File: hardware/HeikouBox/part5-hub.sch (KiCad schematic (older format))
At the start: 43 parts, among them J501 USB_B_Micro, J502 Micro_SD_Card_Det, Q501 MMBT3906, SW501 SW_Push, SW502 SW_Push, SW503 SW_Push, SW504 SW_Push, U501 ATmega644PA-AU, U502 MCP2221AxSL, Y501 8MHz

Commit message: Replace MCU with blue pill, tidy up
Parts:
- removed C501, C505, C506, C509, C511, C512: 100n, Capacitor_SMD:C_0603_1608Metric_Pad1.05x0.95mm_HandSolder, symbol Device:C
- removed C507, C508: 22p, Capacitor_SMD:C_0603_1608Metric_Pad1.05x0.95mm_HandSolder, symbol Device:C
- removed D501: RX, LED_SMD:LED_0603_1608Metric_Pad1.05x0.95mm_HandSolder, symbol Device:LED
- removed D502: TX, LED_SMD:LED_0603_1608Metric_Pad1.05x0.95mm_HandSolder, symbol Device:LED
- removed D503: LOAD, LED_SMD:LED_0603_1608Metric_Pad1.05x0.95mm_HandSolder, symbol Device:LED
- removed J501: USB_B_Micro, KSK_HeikouBox:USB_Mini-Micro-B_Multi, symbol Connector:USB_B_Micro
- removed Q501: MMBT3906, Package_TO_SOT_SMD:SOT-23, symbol Transistor_BJT:MMBT3906
- removed R502, R509: 1K, Resistor_SMD:R_0603_1608Metric_Pad1.05x0.95mm_HandSolder, symbol Device:R
- removed R513: 10K, Resistor_SMD:R_0603_1608Metric_Pad1.05x0.95mm_HandSolder, symbol Device:R
- removed R98: 2K2, Resistor_SMD:R_0603_1608Metric_Pad1.05x0.95mm_HandSolder, symbol Device:R
- removed RN501, RN502: 2K2, Resistor_SMD:R_Array_Convex_4x0603, symbol Device:R_Pack04_Split
- removed SW501: SW_Push, Button_Switch_THT:SW_PUSH_6mm_H5mm, symbol Switch:SW_Push
- removed U501: ATmega644PA-AU, Package_QFP:TQFP-44_10x10mm_P0.8mm, symbol MCU_Microchip_ATmega:ATmega644PA-AU
- removed U502: MCP2221AxSL, Package_SO:SOIC-14_3.9x8.7mm_P1.27mm, symbol Interface_USB:MCP2221AxSL
- removed Y501: 8MHz, Crystal:Crystal_HC49-4H_Vertical, symbol Device:Crystal
- added D501: WS2812B, LED_SMD:LED_WS2812B_PLCC4_5.0x5.0mm_P3.2mm, symbol LED:WS2812B
- added J502: RGB, symbol Connector_Generic:Conn_01x03
- added JP501: Test, symbol Jumper:SolderJumper_2_Open
- added JP502: DVCC, symbol Jumper:SolderJumper_3_Bridged12
- added JP503: DGND, symbol Jumper:SolderJumper_3_Bridged12
- added R502: RUSB, Resistor_SMD:R_0603_1608Metric_Pad1.05x0.95mm_HandSolder, symbol Device:R
- added R502, R504, R506, R515, R517, R519: 1K, Resistor_SMD:R_0603_1608Metric_Pad1.05x0.95mm_HandSolder, symbol Device:R
- added R516, R518: 10K, Resistor_SMD:R_0603_1608Metric_Pad1.05x0.95mm_HandSolder, symbol Device:R
- added R520: 100R, Resistor_SMD:R_0603_1608Metric_Pad1.05x0.95mm_HandSolder, symbol Device:R
- added SW502: Down, Button_Switch_THT:SW_PUSH_6mm_H5mm, symbol Switch:SW_Push
- added U501: STM32-BluePill-Socket, symbol KSK_HeikouBox:STM32-BluePill-Socket
- R509: renamed from R504; value 1K -> 10K
- R510: value 1K -> 2K2
- R511: value 10K -> 2K2
- SW501: renamed from SW502; value SW_Push -> Up
- SW503: value SW_Push -> Left
- SW504: value SW_Push -> Right
- renumbered C510 to C501, J502 to J501, R506 to R513, DS501 to U502
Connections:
- net labels added: cfg_DONE
- net labels removed: gp_CLK, gp_D1, gp_D2, gp_LAT, kb_C, kb_D
- wire segments 164 -> 134
- no-connect marks 8 -> 7
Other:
- note added: "I2C1_SCL"
- note added: "I2C1_SDA"
- note added: "RUSB depends on existing pullup on blue pill!\nNone -> RUSB=1K5\n10K -> RUSB=1K8\n4K7 -> RUSB=2K2\n1K5 -> RUSB=None"
- note added: "SD card"
- note added: "SPI1_MISO"
- note added: "SPI1_MOSI"
- note added: "SPI1_NSS"
- note added: "SPI1_SCK"
- note added: "SPI2_MOSI"
- note added: "SPI2_SCK"
- note added: "STM32 Blue Pill"
- note added: "UART1_RX"
- note added: "UART1_TX"
- note removed: "8M"
- note removed: "Down"
- note removed: "LED PIN"
- note removed: "MISO"
- note removed: "MOSI"
- note removed: "Place near MCP2221"
- note removed: "Place near MCU"
- note removed: "RXD0"
- note removed: "RXD1"
- note removed: "Reset"
- note removed: "SCL"
- note removed: "SD Card"
- note removed: "SDA"
- note removed: "SS"
- note removed: "Select"
- note removed: "TXD0"
- note removed: "TXD1"
- note removed: "USB"
- note removed: "Up"
- note removed: "XCK1"
- moved on the sheet: C501, J501, R509, R512, R513, SW501, U502

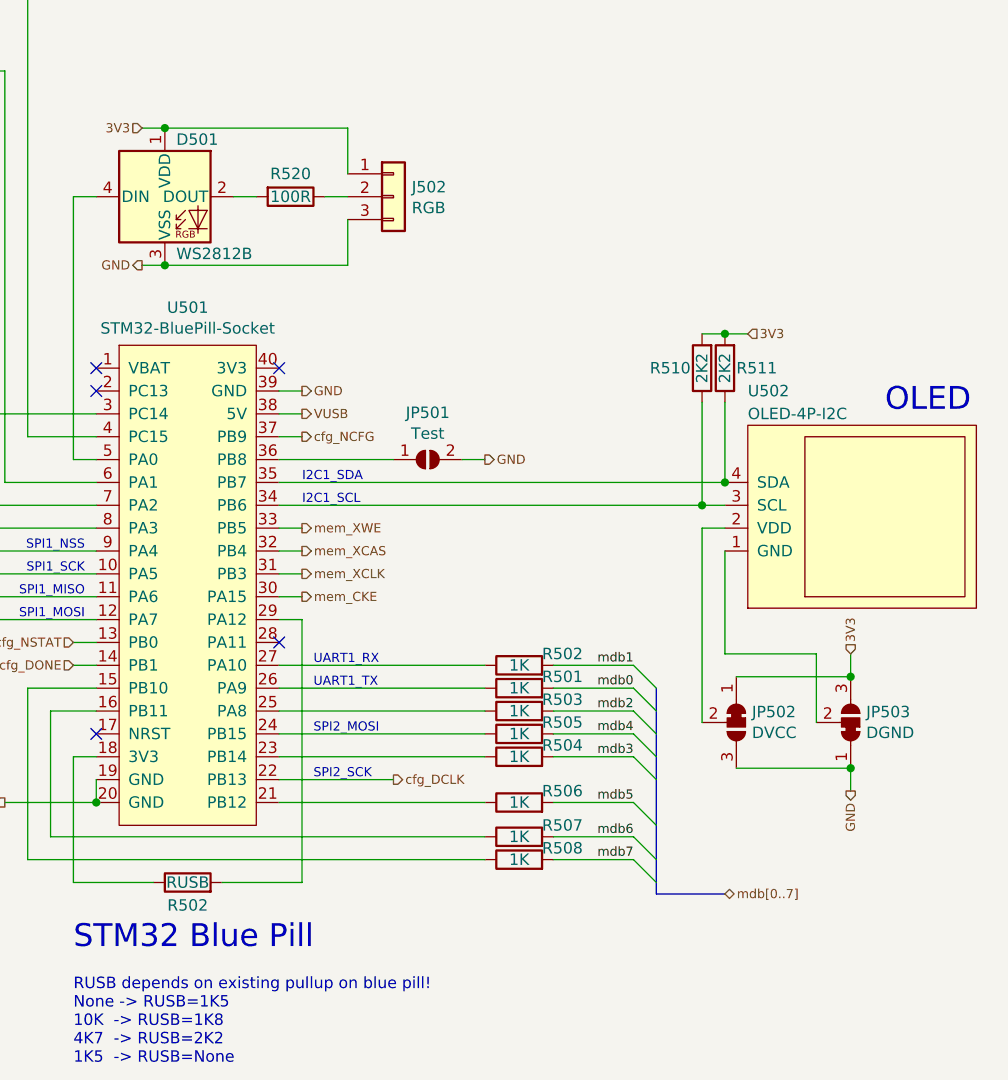
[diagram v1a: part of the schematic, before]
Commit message: Fix DRC, make netlist
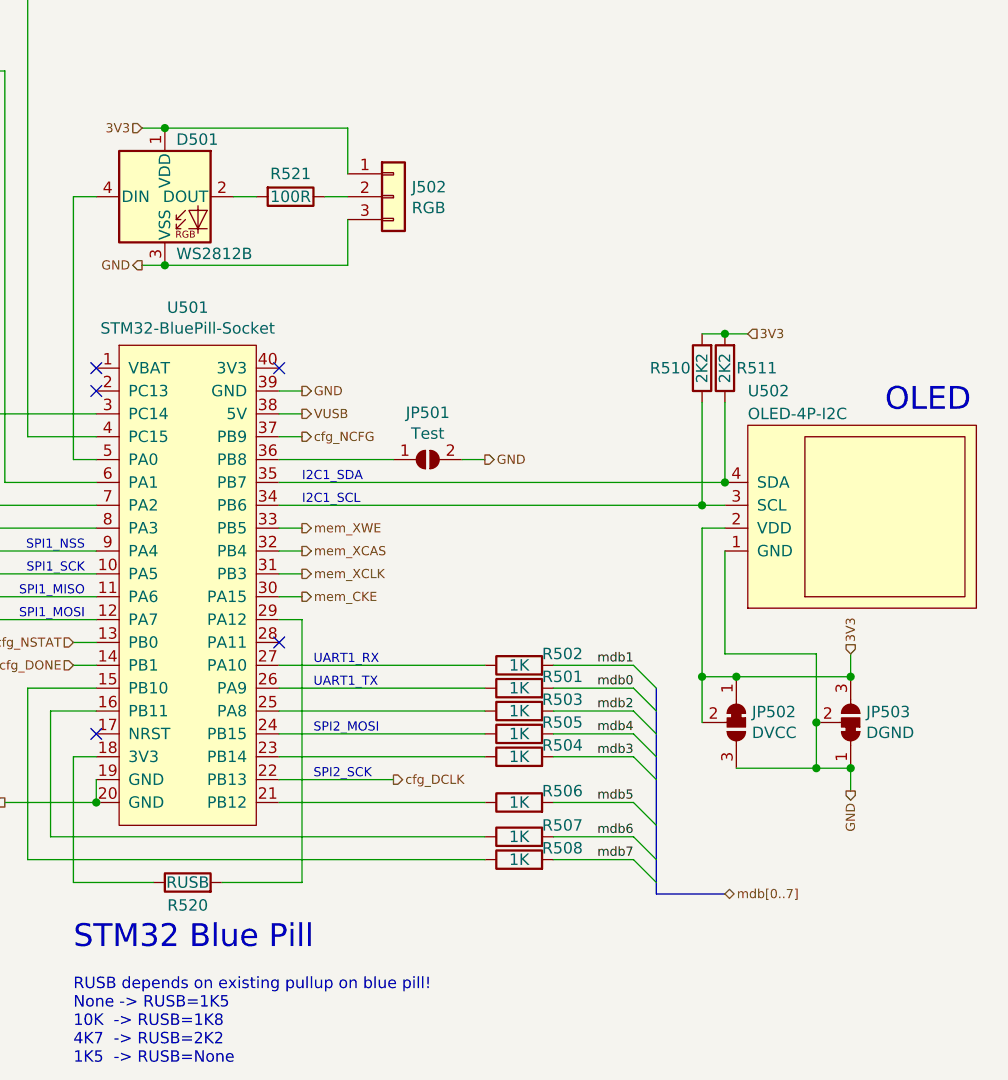
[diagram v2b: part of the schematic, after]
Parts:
- renumbered R502 to R520, R520 to R521
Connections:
- net 3V3: now also JP502.2 (C), U502.2 (VDD)
- net GND: now also JP503.2 (C), U502.1 (GND)
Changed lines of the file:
@@
 $Descr A4 11693 8268
 encoding utf-8
-Sheet 6 6
+Sheet 2 6
 Title "HeikouBox Mainboard - Hub"
 Date "2021-03-17"
@@
 P 4000 4950
 AR Path="/630A62EE" Ref="R?"  Part="1"
-AR Path="/646E3FCF/630A62EE" Ref="R502"  Part="1"
-F 0 "R502" V 3900 4950 50  0000 C CNN
+AR Path="/646E3FCF/630A62EE" Ref="R520"  Part="1"
+F 0 "R520" V 3900 4950 50  0000 C CNN
 F 1 "RUSB" V 4000 4950 50  0000 C CNN
 F 2 "Resistor_SMD:R_0603_1608Metric_Pad1.05x0.95mm_HandSolder" V 3930 4950 50  0001 C CNN
@@
 P 4450 1950
 AR Path="/640DEF09" Ref="R?"  Part="1"
-AR Path="/646E3FCF/640DEF09" Ref="R520"  Part="1"
-F 0 "R520" V 4350 1950 50  0000 C CNN
+AR Path="/646E3FCF/640DEF09" Ref="R521"  Part="1"
+F 0 "R521" V 4350 1950 50  0000 C CNN
 F 1 "100R" V 4450 1950 50  0000 C CNN
 F 2 "Resistor_SMD:R_0603_1608Metric_Pad1.05x0.95mm_HandSolder" V 4380 1950 50  0001 C CNN
@@
 	6400 4050 6900 4050
 Wire Wire Line
-	6400 4450 6900 4450
+	6400 4450 6750 4450
 Connection ~ 6900 4450
 Connection ~ 6900 4050
 Wire Wire Line
-	6250 3400 6250 4250
+	6250 3400 6250 4050
 Wire Wire Line
 	6250 3400 6350 3400
@@
 Wire Wire Line
 	6350 3500 6350 3950
+Wire Wire Line
+	4400 3200 6350 3200
+Wire Wire Line
+	4400 3300 6250 3300
+Wire Wire Line
+	6400 4050 6250 4050
+Connection ~ 6400 4050
+Connection ~ 6250 4050
+Wire Wire Line
+	6250 4050 6250 4250
+Wire Wire Line
+	6750 4250 6750 4450
 Wire Bus Line
 	6050 4100 6050 5000
-Wire Wire Line
-	4400 3200 6350 3200
-Wire Wire Line
-	4400 3300 6250 3300
+Connection ~ 6750 4250
+Connection ~ 6750 4450
+Wire Wire Line
+	6750 4450 6900 4450
 $EndSCHEMATC

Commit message: Mostly routed board
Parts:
- added D502, D503, D504: WS2812B, LED_SMD:LED_WS2812B_PLCC4_5.0x5.0mm_P3.2mm, symbol LED:WS2812B
- added J503: PS/2, KSK_HeikouBox:TE_Mini-DIN-6_Horizontal, symbol KSK_HeikouBox:Mini-DIN-6_Shielded
- added Q501, Q502, Q503: BSS138, Package_TO_SOT_SMD:SOT-23, symbol Transistor_FET:BSS138
- added R522, R523, R524: 1K, Resistor_SMD:R_0603_1608Metric_Pad0.98x0.95mm_HandSolder, symbol Device:R
- added R525, R526, R527, R528: 10K, Resistor_SMD:R_0603_1608Metric_Pad0.98x0.95mm_HandSolder, symbol Device:R
- C501, C502, C503, C504: footprint Capacitor_SMD:C_0603_1608Metric_Pad1.05x0.95mm_HandSolder -> Capacitor_SMD:C_0603_1608Metric_Pad1.08x0.95mm_HandSolder
- DS501: renamed from U502; footprint KSK_HeikouBox:OLED-4P-Generic-128x32-0.91in -> KSK_HeikouBox:OLED-4P-Generic-128x64-0.96in
- J501: value Micro_SD_Card_Det -> Micro_SD_Card_TFP09-2-12B; footprint Connector_Card:microSD_HC_Hirose_DM3D-SF -> KSK_HeikouBox:Micro_SD_Card_TFP09-2-12B; symbol Connector:Micro_SD_Card_Det -> KSK_HeikouBox:Micro_SD_Card_TFP09-2-12B
- J502: footprint (none) -> Connector_PinHeader_2.54mm:PinHeader_1x03_P2.54mm_Vertical
- JP501: value Test -> RGB Bypass; footprint (none) -> Jumper:SolderJumper-2_P1.3mm_Open_RoundedPad1.0x1.5mm
- JP502, JP503: footprint (none) -> Jumper:SolderJumper-3_P1.3mm_Open_RoundedPad1.0x1.5mm; symbol Jumper:SolderJumper_3_Bridged12 -> Jumper:SolderJumper_3_Open
- R501, R502, R503, R504, R505, R506, R507, R508, R509, R510, R511, R512, R513, R514, R515, R516, R517, R518, R519, R520: footprint Resistor_SMD:R_0603_1608Metric_Pad1.05x0.95mm_HandSolder -> Resistor_SMD:R_0603_1608Metric_Pad0.98x0.95mm_HandSolder
- R521: value 100R -> 1K; footprint Resistor_SMD:R_0603_1608Metric_Pad1.05x0.95mm_HandSolder -> Resistor_SMD:R_0603_1608Metric_Pad0.98x0.95mm_HandSolder
- SW501: value Up -> Left
- SW502: value Down -> Up
- SW503: value Left -> Down
- U501: footprint (none) -> KSK_HeikouBox:STM32-BluePill-Socket
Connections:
- net 3V3: now also R512.1, R514.1, R516.1, R518.1, R520.2, R521.2, Q501.1 (G), Q502.1 (G), Q503.1 (G), R525.2, R527.2; no longer D501.1 (VDD), DS501.2 (VDD), J502.1 (Pin_1), JP502.2 (C), R512.2, R514.2, R516.2, R518.2
- net GND: now also SW501.2, SW502.2, SW503.2, SW504.2, D502.3 (VSS), D503.3 (VSS), D504.3 (VSS), J503.3, J503.SH; no longer DS501.1 (GND), J501.10 (DET_A), J501.11 (SHIELD), JP501.2 (B), JP503.2 (C), R513.1, R515.1, R517.1, R519.1
- net cfg_DONE: now also U501.32 (PB4); no longer U501.14 (PB1)
- net cfg_NSTAT: now also U501.33 (PB5); no longer U501.13 (PB0)
- net mem_XCAS: now also U501.31 (PB3); no longer U501.32 (PB4)
- net mem_XCLK: now also U501.13 (PB0); no longer U501.31 (PB3)
- net mem_XWE: now also U501.14 (PB1); no longer U501.33 (PB5)
- net at U501.18 (3V3): no longer R520.1
- net at U501.2 (PC13): now also Q502.2 (S), R525.1
- net at U501.29 (PA12): now also R520.1; no longer R520.2
- net at U501.36 (PB8): now also Q503.2 (S), R527.1; no longer JP501.1 (A)
- net at C501.2, U501.4 (PC15): now also R512.2, R513.2; no longer R512.1, SW501.1
- net at U501.5 (PA0): now also R521.1, Q501.2 (S); no longer D501.4 (DIN)
- net at C502.2, U501.6 (PA1): now also R514.2, R515.2; no longer R514.1, SW502.1
- net at C503.2, U501.7 (PA2): now also R516.2, R517.2; no longer R516.1, SW503.1
- net at C504.2, U501.8 (PA3): now also R518.2, R519.2; no longer R518.1, SW504.1
- net at D501.2 (DOUT): now also D502.4 (DIN); no longer R521.2
- net at J502.2 (Pin_2): now also JP501.2 (B), R524.2; no longer R521.1
- new net: J503.1, Q502.3 (D), R526.1
- new net: J503.5, Q503.3 (D), R528.1
- new net: D502.2 (DOUT), D503.4 (DIN)
- new net: D503.2 (DOUT), D504.4 (DIN)
- new net: D504.2 (DOUT), R524.1
- new net: R515.1, SW502.1
- new net: R517.1, SW503.1
- new net: R519.1, SW504.1
- new net: Q501.3 (D), R522.1, R523.1
- new net: D501.4 (DIN), JP501.1 (A), R523.2
- new net: DS501.2 (VDD), JP502.2 (C)
- new net: DS501.1 (GND), JP503.2 (C)
- new net: R513.1, SW501.1
- new net 5V: D501.1 (VDD), D502.1 (VDD), D503.1 (VDD), D504.1 (VDD), J502.1 (Pin_1), J503.4, R522.2, R526.2, R528.2
- no-connect marks 7 -> 9
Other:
- note added: "Gamer RGB go-faster lights"
- note added: "Keyboard"
- note added: "PS/2 Clock"
- note added: "PS/2 Data"
- moved on the sheet: C501, C502, C503, C504, D501, DS501, J502, R501, R502, R503, R504, R505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

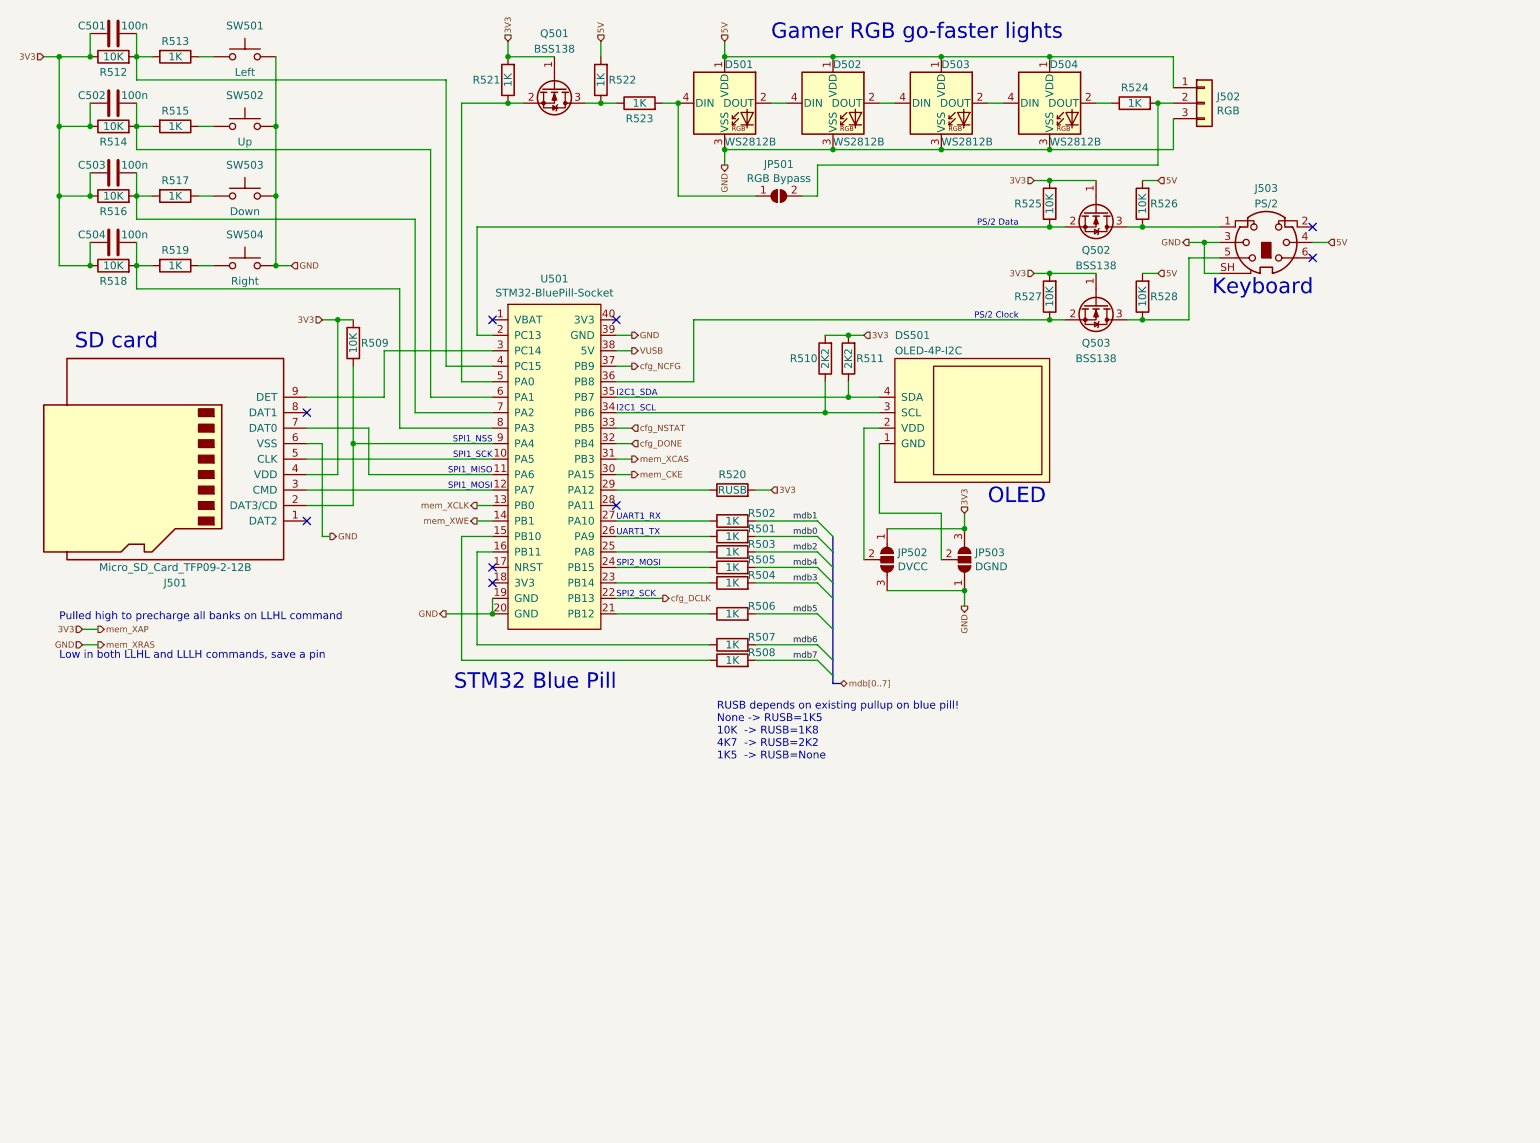
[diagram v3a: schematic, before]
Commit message: Rerouted some logic
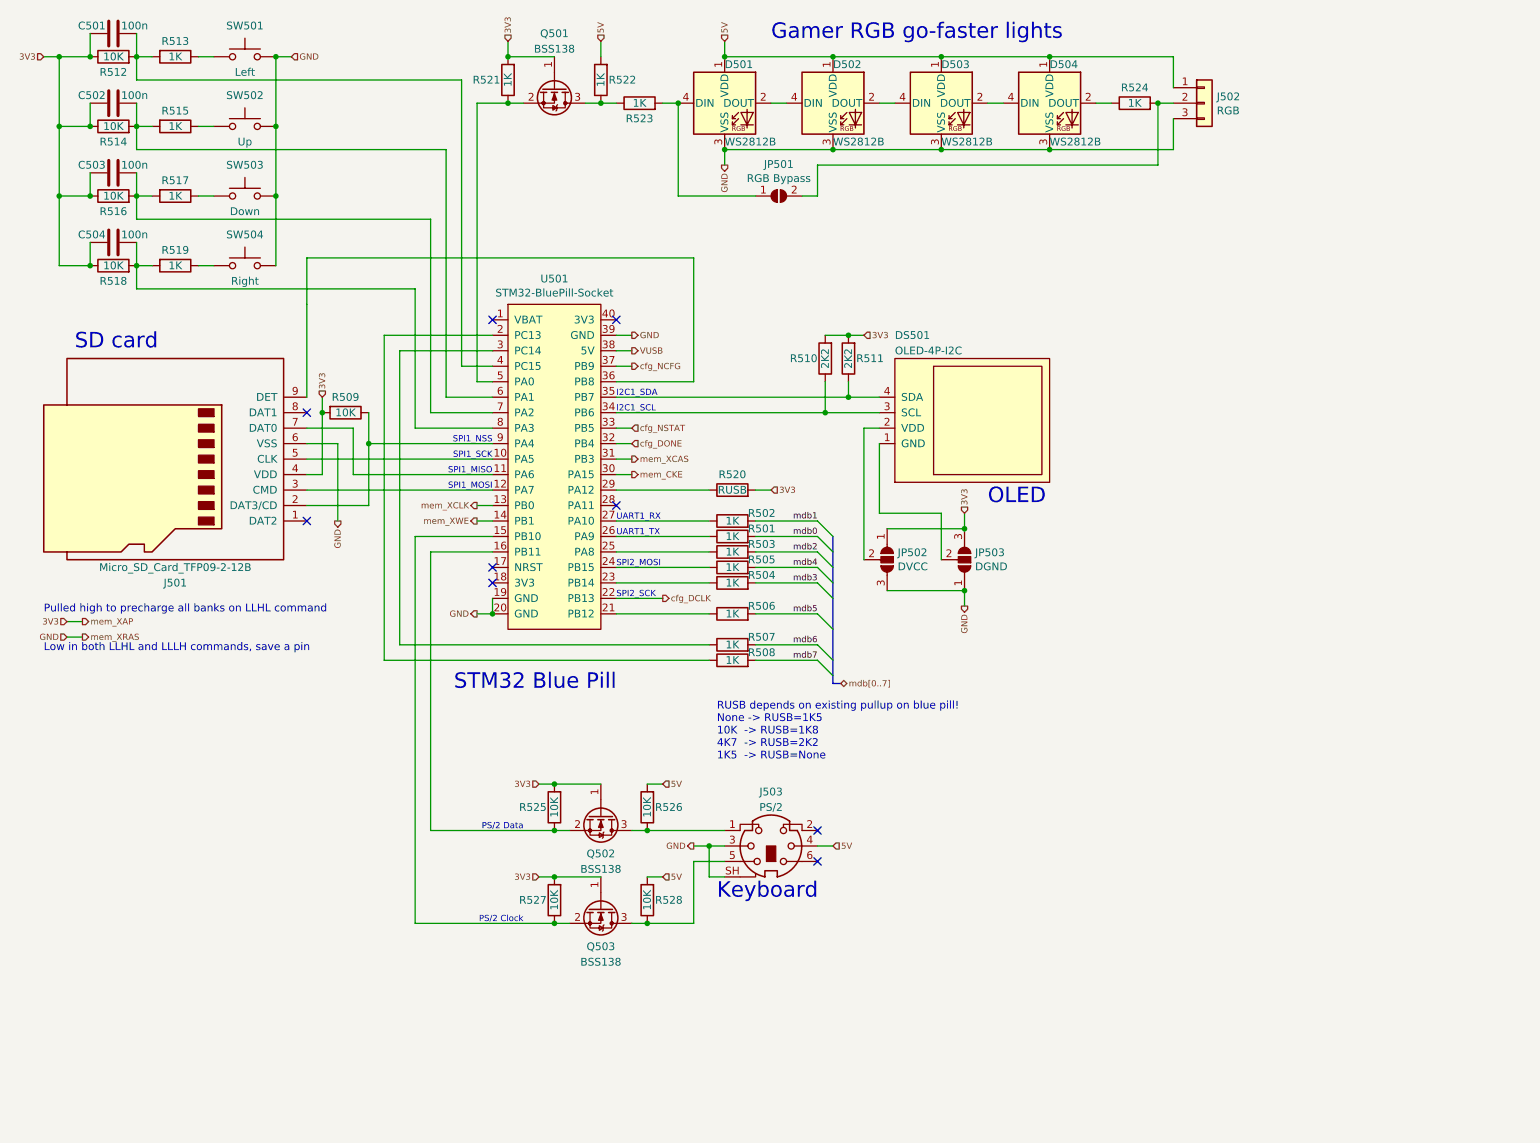
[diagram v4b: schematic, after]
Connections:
- net at U501.15 (PB10): now also Q503.2 (S), R527.1; no longer R508.1
- net at U501.16 (PB11): now also Q502.2 (S), R525.1; no longer R507.1
- net at U501.3 (PC14): now also R507.1; no longer J501.9 (DET)
- new net: R508.1, U501.2 (PC13)
- new net: J501.9 (DET), U501.36 (PB8)
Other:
- moved on the sheet: J503, Q502, Q503, R509, R525, R526, R527, R528
